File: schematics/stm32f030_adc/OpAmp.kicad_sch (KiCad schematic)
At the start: 18 parts, among them U3 TL072, U5 TL072

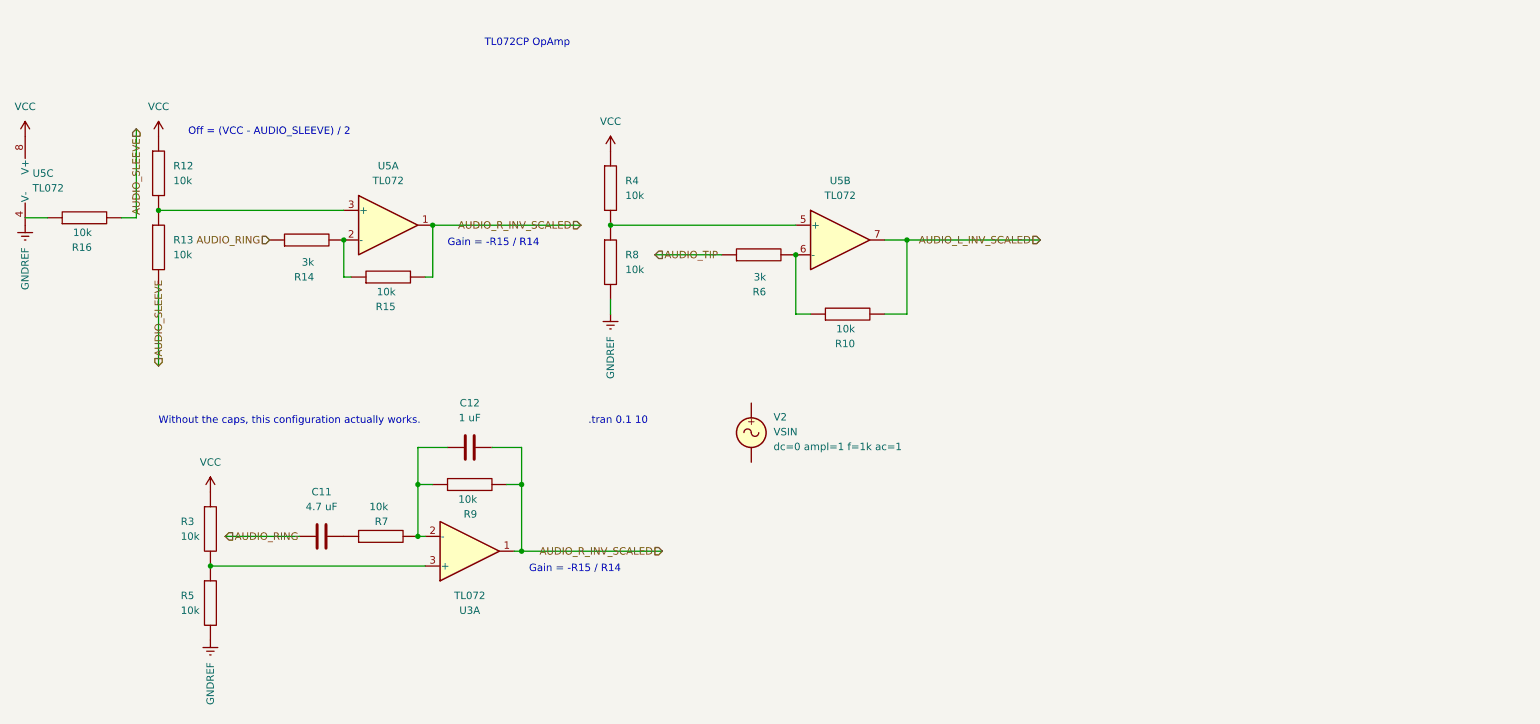
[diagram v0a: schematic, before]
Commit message: [schematics:*] Bug | Fixed OpAmp schematics based on the simulation and practical experiments' results
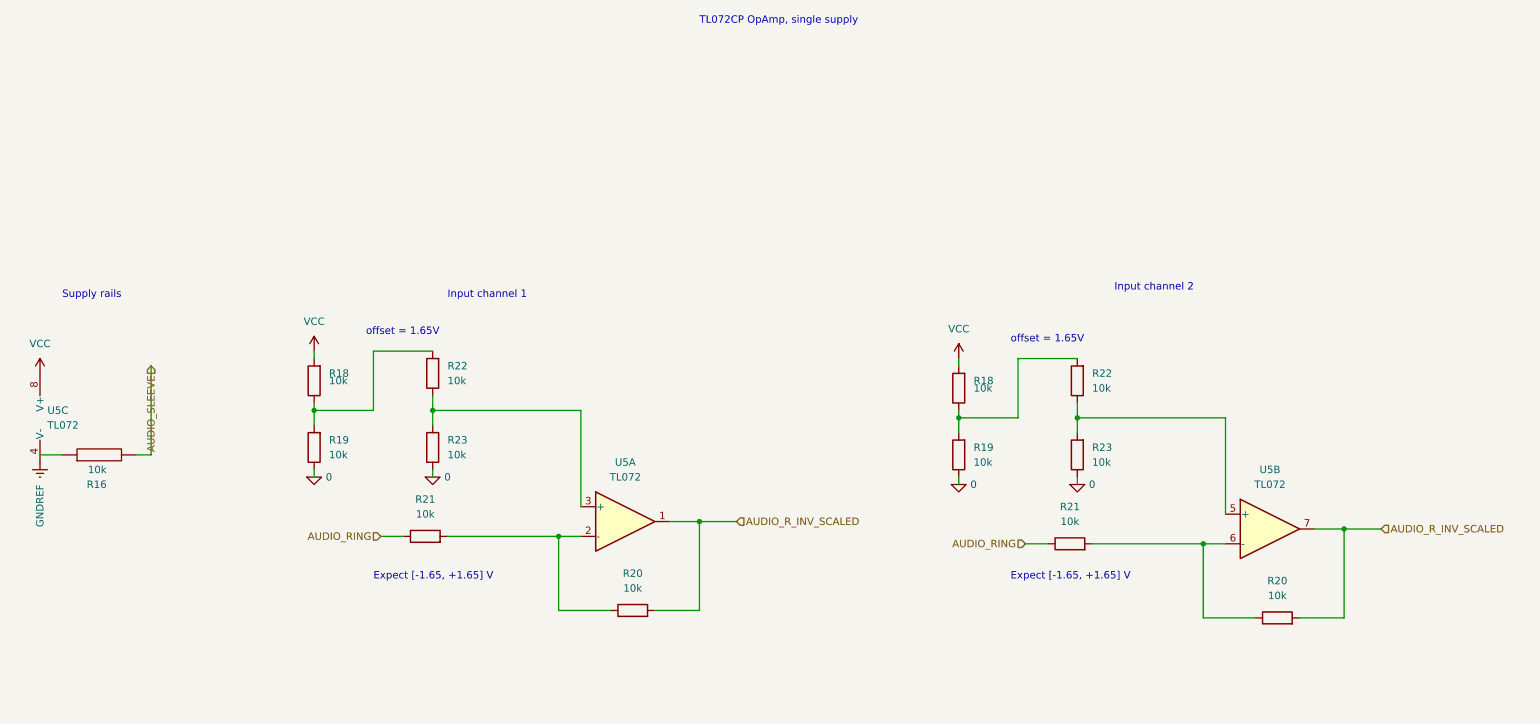
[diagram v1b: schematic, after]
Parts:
- removed C11: 4.7 uF, symbol Device:C
- removed C12: 1 uF, symbol Device:C
- removed R10, R12, R13, R15, R3, R4, R5, R7, R8, R9: 10k, symbol pspice:R
- removed R14, R6: 3k, symbol pspice:R
- removed U3: TL072, symbol Amplifier_Operational:TL072
- removed V2: VSIN, symbol Simulation_SPICE:VSIN
- added R18 (x2), R19 (x2), R20 (x2), R21 (x2), R22 (x2), R23 (x2): 10k, symbol Device:R
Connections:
- net AUDIO_L_INV_SCALED is gone; now on net AUDIO_R_INV_SCALED: U5.7
- net AUDIO_RING: now also R21.1, R21.1
- net AUDIO_R_INV_SCALED: now also R20.2, R20.2
- net VCC: now also R18.2, R18.2
- net at U5.5 (+): now also R22.1, R23.2
- net at U5.6 (-): now also R20.1, R21.2
- net at U5.3 (+): now also R22.1, R23.2
- net at U5.2 (-): now also R20.1, R21.2
- new net: R18.1, R19.2, R22.2 (x2)
- new net 0: R19.1, R19.1, R23.1, R23.1
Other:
- note added: "Expect [-1.65, +1.65] V"
- note added: "Input channel 1"
- note added: "Input channel 2"
- note added: "Supply rails"
- note added: "TL072CP OpAmp, single supply"
- note added: "offset = 1.65V"
- note removed: ".tran 0.1 10"
- note removed: "Gain = -R15 / R14"
- note removed: "Off = (VCC - AUDIO_SLEEVE) / 2"
- note removed: "TL072CP OpAmp"
- note removed: "Without the caps, this configuration actually works."
- moved on the sheet: R16, U5A, U5B, U5C

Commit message: [stm32f030_adc:OpAmp] Impl | Accumulated changes
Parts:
- added C11: 10 uF, symbol Device:C
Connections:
- net AUDIO_RING: now also C11.2; no longer R21.1
- net at R20.1, U5.2 (-): now also R21.1; no longer R21.2
- new net: C11.1, R21.2
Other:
- moved on the sheet: R21
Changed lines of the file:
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@@
     (stroke (width 0) (type default))
   )
-  (wire (pts (xy 83.82 110.49) (xy 87.63 110.49))
+  (wire (pts (xy 73.66 110.49) (xy 80.01 110.49))
     (stroke (width 0) (type default))
   )
@@
     (stroke (width 0) (type default))
   )
-  (wire (pts (xy 138.43 107.95) (xy 144.78 107.95))
+  (wire (pts (xy 138.43 107.95) (xy 147.32 107.95))
     (stroke (width 0) (type default))
   )
@@
     (stroke (width 0) (type default))
   )
-  (wire (pts (xy 95.25 110.49) (xy 114.3 110.49))
+  (wire (pts (xy 87.63 110.49) (xy 96.52 110.49))
     (stroke (width 0) (type default))
   )
@@
     (stroke (width 0) (type default))
   )
-  (wire (pts (xy 114.3 123.19) (xy 114.3 110.49))
+  (wire (pts (xy 114.3 110.49) (xy 114.3 123.19))
     (stroke (width 0) (type default))
   )
@@
   )
   (wire (pts (xy 233.68 124.46) (xy 224.79 124.46))
+    (stroke (width 0) (type default))
+  )
+  (wire (pts (xy 104.14 110.49) (xy 114.3 110.49))
     (stroke (width 0) (type default))
   )
@@
     (effects (font (size 1.27 1.27)) (justify left))
   )
-  (hierarchical_label "AUDIO_R_INV_SCALED" (shape input) (at 144.78 107.95 0) (fields_autoplaced)
+  (hierarchical_label "AUDIO_R_INV_SCALED" (shape input) (at 147.32 107.95 0) (fields_autoplaced)
     (effects (font (size 1.27 1.27)) (justify left))
   )
@@
     (effects (font (size 1.27 1.27)) (justify right))
   )
-  (hierarchical_label "AUDIO_RING" (shape input) (at 83.82 110.49 180) (fields_autoplaced)
+  (hierarchical_label "AUDIO_RING" (shape input) (at 73.66 110.49 180) (fields_autoplaced)
     (effects (font (size 1.27 1.27)) (justify right))
   )
@@
     )
   )
+  (symbol (lib_id "Device:C") (at 83.82 110.49 270) (mirror x) (unit 1)
+    (in_bom yes) (on_board yes) (dnp no) (fields_autoplaced)
+    (property "Reference" "C11" (at 83.82 102.87 90)
+      (effects (font (size 1.27 1.27)))
+    )
+    (property "Value" "10 uF" (at 83.82 105.41 90)
+      (effects (font (size 1.27 1.27)))
+    )
+    (property "Footprint" "" (at 80.01 109.5248 0)
+      (effects (font (size 1.27 1.27)) hide)
+    )
+    (property "Datasheet" "~" (at 83.82 110.49 0)
+      (effects (font (size 1.27 1.27)) hide)
+    )
+    (pin "1")
+    (pin "2")
+    (instances
+      (project "stm32f030_adc"
+        (path "/85629656-c73b-4e1f-b8e8-4366f4b01266/b4185304-bcce-4cb1-98f3-8bffc8e76c1e"
+          (reference "C11") (unit 1)
+        )
+      )
+    )
+  )
   (symbol (lib_id "Amplifier_Operational:TL072") (at 27.94 90.17 0) (unit 3)
     (in_bom yes) (on_board yes) (dnp no) (fields_autoplaced)
@@
     )
   )
-  (symbol (lib_id "Device:R") (at 91.44 110.49 90) (unit 1)
-    (in_bom yes) (on_board yes) (dnp no) (fields_autoplaced)
-    (property "Reference" "R21" (at 91.44 104.14 90)
-      (effects (font (size 1.27 1.27)))
-    )
-    (property "Value" "10k" (at 91.44 106.68 90)
-      (effects (font (size 1.27 1.27)))
-    )
-    (property "Footprint" "" (at 91.44 112.268 90)
-      (effects (font (size 1.27 1.27)) hide)
-    )
-    (property "Datasheet" "~" (at 91.44 110.49 0)
-      (effects (font (size 1.27 1.27)) hide)
-    )
+  (symbol (lib_id "Device:R") (at 100.33 110.49 270) (mirror x) (unit 1)
+    (in_bom yes) (on_board yes) (dnp no) (fields_autoplaced)
+    (property "Reference" "R21" (at 100.33 104.14 90)
+      (effects (font (size 1.27 1.27)))
+    )
+    (property "Value" "10k" (at 100.33 106.68 90)
+      (effects (font (size 1.27 1.27)))
+    )
+    (property "Footprint" "" (at 100.33 112.268 90)
+      (effects (font (size 1.27 1.27)) hide)
+    )
+    (property "Datasheet" "~" (at 100.33 110.49 0)
+      (effects (font (size 1.27 1.27)) hide)
+    )

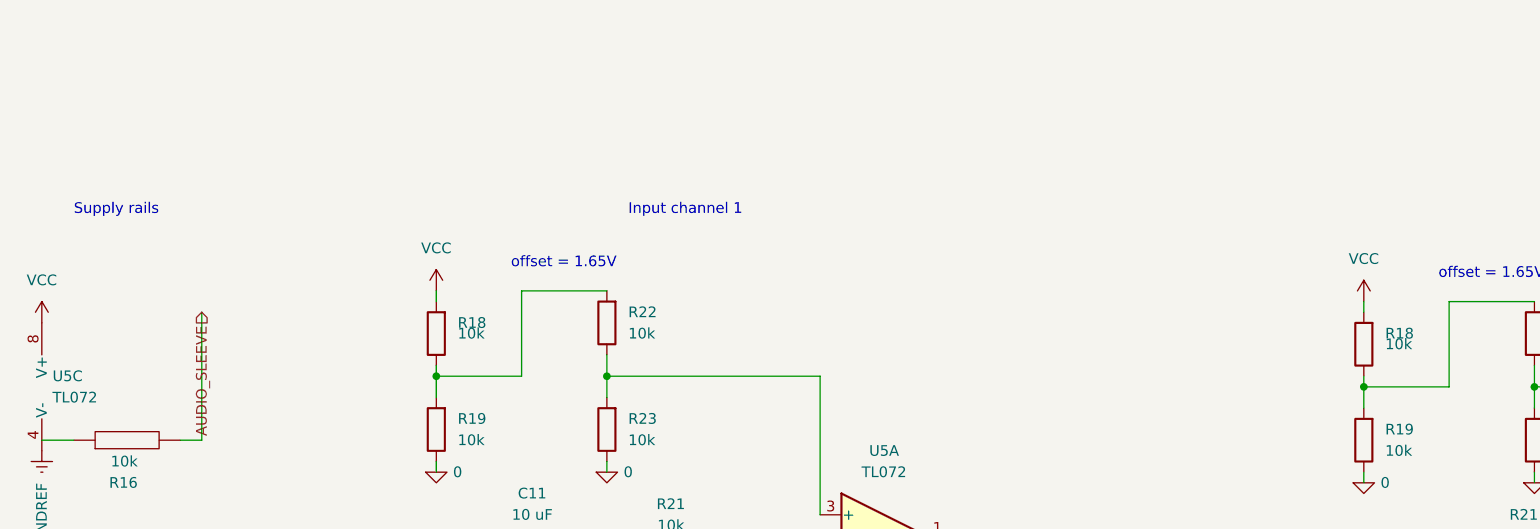
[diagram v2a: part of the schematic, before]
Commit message: [stm32f030_adc:OpAmp] Bug | 3V3 / VCC -- confused symbols
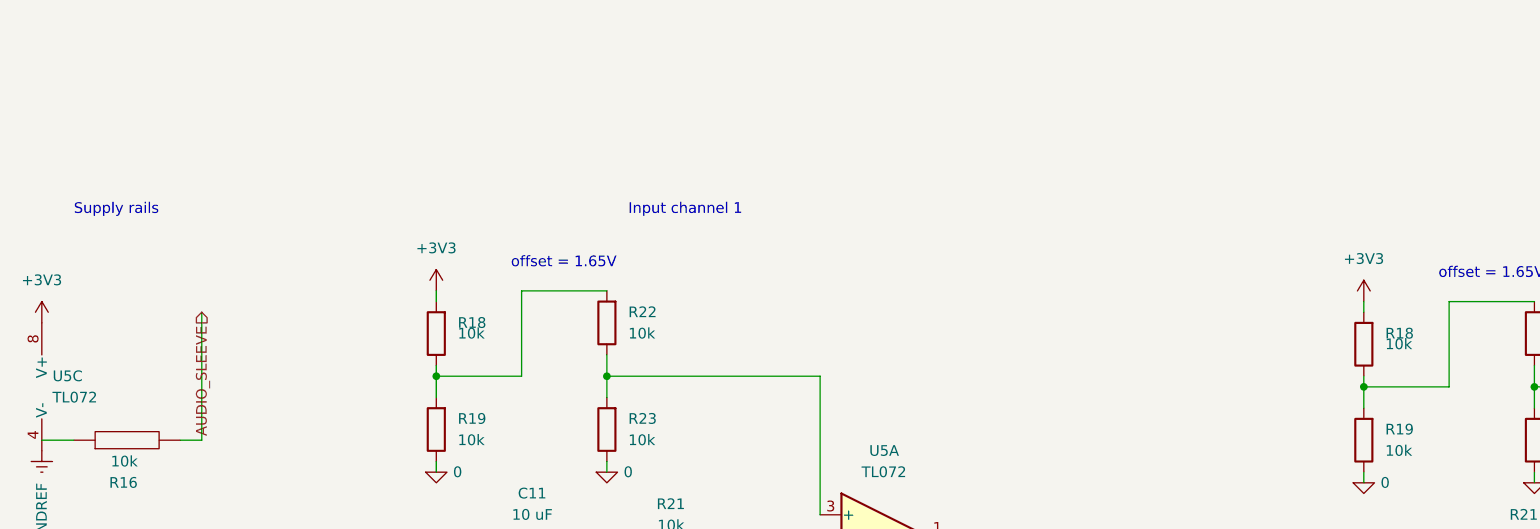
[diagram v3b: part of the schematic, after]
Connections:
- net VCC renamed +3V3
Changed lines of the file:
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@@
-    )
-  )
-  (symbol (lib_id "power:VCC") (at 182.88 80.01 0) (unit 1)
-    (in_bom yes) (on_board yes) (dnp no)
-    (property "Reference" "#PWR04" (at 182.88 83.82 0)
-      (effects (font (size 1.27 1.27)) hide)
-    )
-    (property "Value" "VCC" (at 182.88 74.93 0)
-      (effects (font (size 1.27 1.27)))
-    )
-    (property "Footprint" "" (at 182.88 80.01 0)
-      (effects (font (size 1.27 1.27)) hide)
-    )
-    (property "Datasheet" "" (at 182.88 80.01 0)
-      (effects (font (size 1.27 1.27)) hide)
-    )
-    (pin "1")
-    (instances
-      (project "stm32f030_adc"
-        (path "/85629656-c73b-4e1f-b8e8-4366f4b01266"
-          (reference "#PWR04") (unit 1)
-        )
-        (path "/85629656-c73b-4e1f-b8e8-4366f4b01266/b4185304-bcce-4cb1-98f3-8bffc8e76c1e"
-          (reference "#PWR010") (unit 1)
-        )
-      )
     )
   )
@@
     )
   )
-  (symbol (lib_id "power:VCC") (at 25.4 82.55 0) (unit 1)
-    (in_bom yes) (on_board yes) (dnp no)
-    (property "Reference" "#PWR04" (at 25.4 86.36 0)
-      (effects (font (size 1.27 1.27)) hide)
-    )
-    (property "Value" "VCC" (at 25.4 77.47 0)
-      (effects (font (size 1.27 1.27)))
-    )
-    (property "Footprint" "" (at 25.4 82.55 0)
-      (effects (font (size 1.27 1.27)) hide)
-    )
-    (property "Datasheet" "" (at 25.4 82.55 0)
+  (symbol (lib_id "power:+3V3") (at 182.88 80.01 0) (unit 1)
+    (in_bom yes) (on_board yes) (dnp no) (fields_autoplaced)
+    (property "Reference" "#PWR0104" (at 182.88 83.82 0)
+      (effects (font (size 1.27 1.27)) hide)
+    )
+    (property "Value" "+3V3" (at 182.88 74.93 0)
+      (effects (font (size 1.27 1.27)))
+    )
+    (property "Footprint" "" (at 182.88 80.01 0)
+      (effects (font (size 1.27 1.27)) hide)
+    )
+    (property "Datasheet" "" (at 182.88 80.01 0)
       (effects (font (size 1.27 1.27)) hide)
     )
@@
       (project "stm32f030_adc"
         (path "/85629656-c73b-4e1f-b8e8-4366f4b01266"
-          (reference "#PWR04") (unit 1)
+          (reference "#PWR0104") (unit 1)
         )
         (path "/85629656-c73b-4e1f-b8e8-4366f4b01266/b4185304-bcce-4cb1-98f3-8bffc8e76c1e"
@@
     )
   )
-  (symbol (lib_id "power:VCC") (at 72.39 78.74 0) (unit 1)
-    (in_bom yes) (on_board yes) (dnp no)
-    (property "Reference" "#PWR04" (at 72.39 82.55 0)
-      (effects (font (size 1.27 1.27)) hide)
-    )
-    (property "Value" "VCC" (at 72.39 73.66 0)
+  (symbol (lib_id "power:+3V3") (at 72.39 78.74 0) (unit 1)
+    (in_bom yes) (on_board yes) (dnp no) (fields_autoplaced)
+    (property "Reference" "#PWR0104" (at 72.39 82.55 0)
+      (effects (font (size 1.27 1.27)) hide)
+    )
+    (property "Value" "+3V3" (at 72.39 73.66 0)
       (effects (font (size 1.27 1.27)))
     )
@@
       (project "stm32f030_adc"
         (path "/85629656-c73b-4e1f-b8e8-4366f4b01266"
-          (reference "#PWR04") (unit 1)
-        )
-        (path "/85629656-c73b-4e1f-b8e8-4366f4b01266/b4185304-bcce-4cb1-98f3-8bffc8e76c1e"
-          (reference "#PWR09") (unit 1)
+          (reference "#PWR0104") (unit 1)
+        )
+        (path "/85629656-c73b-4e1f-b8e8-4366f4b01266/b4185304-bcce-4cb1-98f3-8bffc8e76c1e"
+          (reference "#PWR06") (unit 1)
         )
       )
@@
         )
       )
+    )
+  )
+  (symbol (lib_id "power:+3V3") (at 25.4 82.55 0) (unit 1)
+    (in_bom yes) (on_board yes) (dnp no) (fields_autoplaced)
+    (property "Reference" "#PWR0104" (at 25.4 86.36 0)
+      (effects (font (size 1.27 1.27)) hide)
+    )
+    (property "Value" "+3V3" (at 25.4 77.47 0)
+      (effects (font (size 1.27 1.27)))
+    )
+    (property "Footprint" "" (at 25.4 82.55 0)
+      (effects (font (size 1.27 1.27)) hide)
+    )
+    (property "Datasheet" "" (at 25.4 82.55 0)
+      (effects (font (size 1.27 1.27)) hide)
+    )
+    (pin "1")
+    (instances
+      (project "stm32f030_adc"
+        (path "/85629656-c73b-4e1f-b8e8-4366f4b01266"
+          (reference "#PWR0104") (unit 1)
+        )
+        (path "/85629656-c73b-4e1f-b8e8-4366f4b01266/b4185304-bcce-4cb1-98f3-8bffc8e76c1e"
+          (reference "#PWR07") (unit 1)
+        )
+      )
